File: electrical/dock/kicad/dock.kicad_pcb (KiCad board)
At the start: 4 copper layers, 160 x 100 mm, 9 parts, among them J1 USBC_UP, J5 RJ45, J6 POGO, U1 JHL9040, U2 TPS65994, U3 RTL8156, U4 VL817, U5 TPS55288, U8 DWM3001C

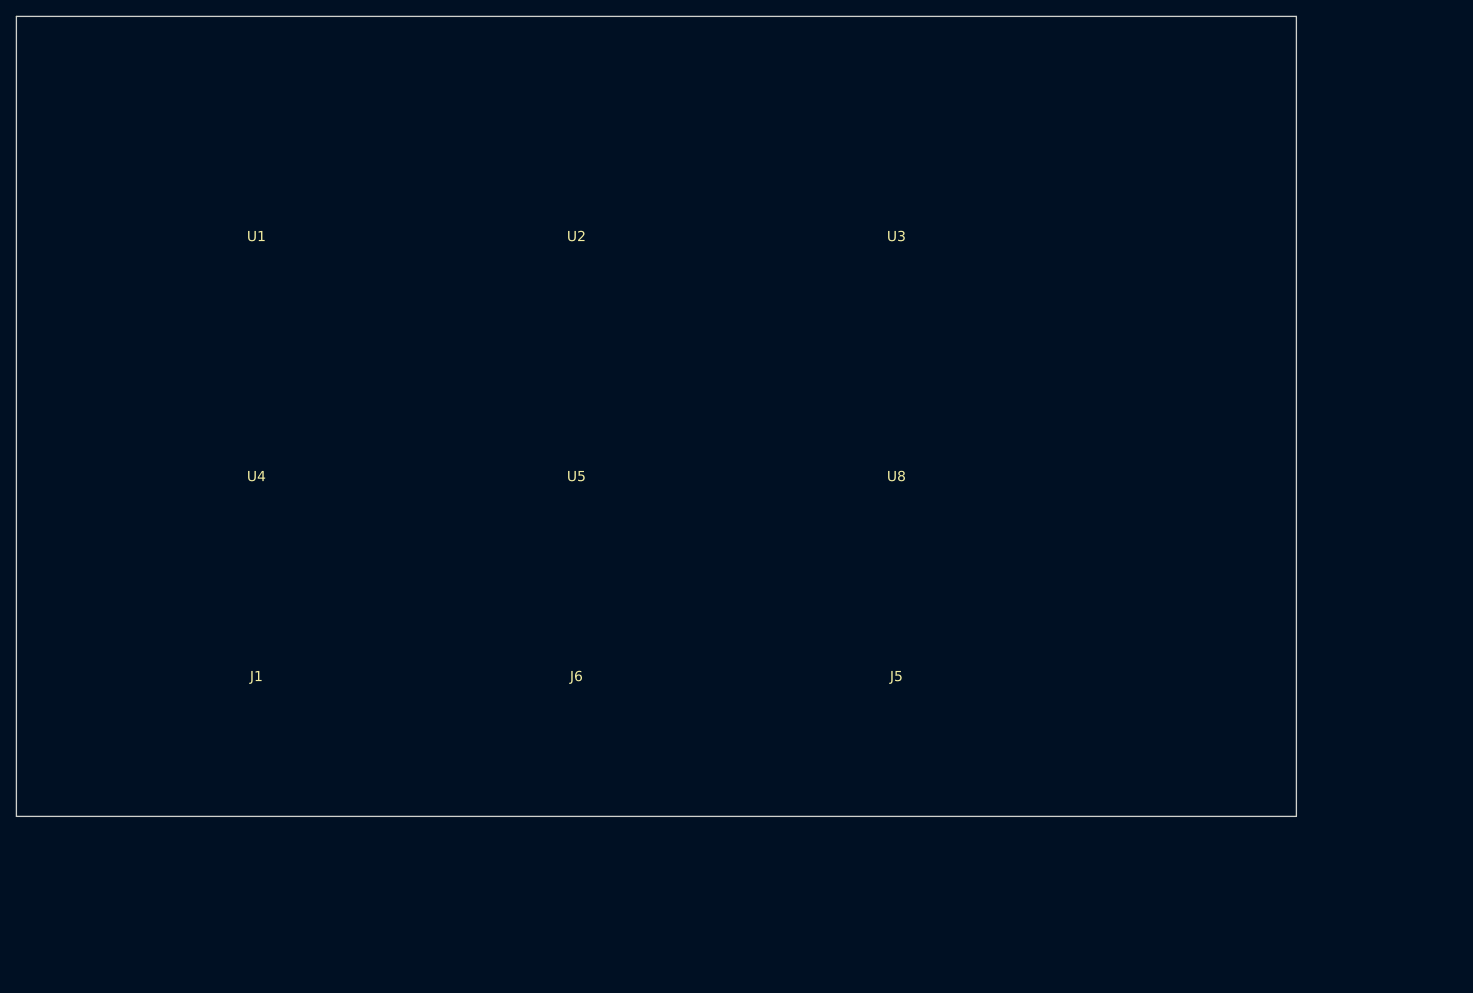
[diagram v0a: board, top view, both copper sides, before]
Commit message: feat(eda): Cont VII release-clean ledger + ERC/DRC zero-error revalidation
Investigate every Cont VI ERC/DRC entry, wire functional nets, clear error-class
violations, and publish honest release-clean tokens (CLI pass ≠ clean pass).

Co-authored-by: Cursor <cursoragent@cursor.com>
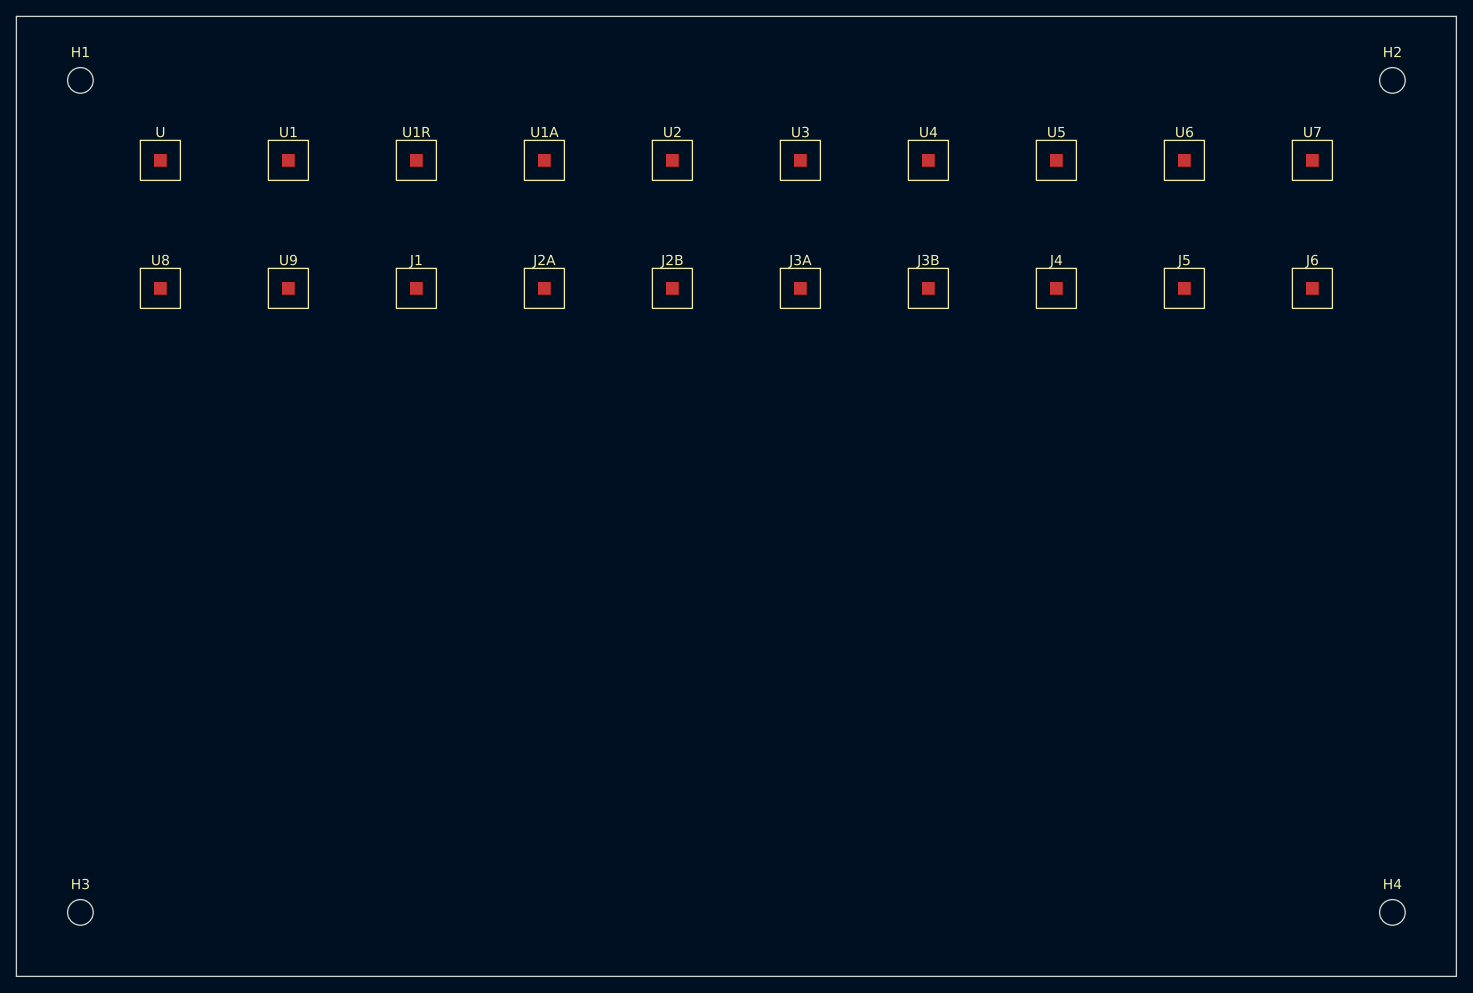
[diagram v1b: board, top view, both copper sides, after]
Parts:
- added H1: M3, gunnchos_structural:MountingHole_3.2mm, F.Cu at (8.00, 8.00)
- added H2: M3, gunnchos_structural:MountingHole_3.2mm, F.Cu at (172.0, 8.00)
- added H3: M3, gunnchos_structural:MountingHole_3.2mm, F.Cu at (8.00, 112.0)
- added H4: M3, gunnchos_structural:MountingHole_3.2mm, F.Cu at (172.0, 112.0)
- added J2A: USB4085, gunnchos_structural:Block_SMD_10x10, F.Cu at (66.0, 34.0)
- added J2B: USB4085, gunnchos_structural:Block_SMD_10x10, F.Cu at (82.0, 34.0)
- added J3A: USB3_A, gunnchos_structural:Block_SMD_10x10, F.Cu at (98.0, 34.0)
- added J3B: USB3_A, gunnchos_structural:Block_SMD_10x10, F.Cu at (114.0, 34.0)
- added J4: HDMI_TypeA, gunnchos_structural:Block_SMD_10x10, F.Cu at (130.0, 34.0)
- added U: FuncBlock, gunnchos_structural:Block_SMD_10x10, F.Cu at (18.0, 18.0)
- added U1A: VL108, gunnchos_structural:Block_SMD_10x10, F.Cu at (66.0, 18.0)
- added U1R: JHL9040R, gunnchos_structural:Block_SMD_10x10, F.Cu at (50.0, 18.0)
- added U6: TPS62864, gunnchos_structural:Block_SMD_10x10, F.Cu at (146.0, 18.0)
- added U7: TLV75533PDRVR, gunnchos_structural:Block_SMD_10x10, F.Cu at (162.0, 18.0)
- added U9: ALC4050, gunnchos_structural:Block_SMD_10x10, F.Cu at (34.0, 34.0)
- J1: value USBC_UP -> USB4085; footprint Package_DFN_QFN:QFN-48-1EP_7x7mm_P0.5mm -> gunnchos_structural:Block_SMD_10x10
- J5: value RJ45 -> JK0-0136NL; footprint Package_DFN_QFN:QFN-48-1EP_7x7mm_P0.5mm -> gunnchos_structural:Block_SMD_10x10
- J6: value POGO -> Mill-Max_pogo; footprint Package_DFN_QFN:QFN-48-1EP_7x7mm_P0.5mm -> gunnchos_structural:Block_SMD_10x10
- U1: value JHL9040 -> JHL8440; footprint Package_DFN_QFN:QFN-48-1EP_7x7mm_P0.5mm -> gunnchos_structural:Block_SMD_10x10
- U2: value TPS65994 -> TPS65994ADFBRQ1; footprint Package_DFN_QFN:QFN-48-1EP_7x7mm_P0.5mm -> gunnchos_structural:Block_SMD_10x10
- U3, U4, U8: footprint Package_DFN_QFN:QFN-48-1EP_7x7mm_P0.5mm -> gunnchos_structural:Block_SMD_10x10
- U5: value TPS55288 -> TPS55288RPMR; footprint Package_DFN_QFN:QFN-48-1EP_7x7mm_P0.5mm -> gunnchos_structural:Block_SMD_10x10
- moved J6 105.2 mm to (162.0, 34.0)
- moved U8 95.6 mm to (18.0, 34.0)
- moved U4 93.9 mm to (114.0, 18.0)
- moved U5 73.2 mm to (130.0, 18.0)
- moved J5 62.4 mm to (146.0, 34.0)
- moved J1 54.8 mm to (50.0, 34.0)
- moved U2 17.0 mm to (82.0, 18.0)
- moved U3 17.0 mm to (98.0, 18.0)
- moved U1 12.6 mm to (34.0, 18.0)
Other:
- board size 160 x 100 mm -> 180 x 120 mm
- rule pad_to_mask_clearance: 0.051 -> 0.0
